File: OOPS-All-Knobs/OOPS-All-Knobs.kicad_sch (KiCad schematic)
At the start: 144 parts

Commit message: Added ground
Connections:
- net GND: now reaches ENC24.C
- net GND: now also ENC1.C, ENC10.C, ENC11.C, ENC12.C, ENC13.C, ENC14.C, ENC15.C, ENC16.C, ENC17.C, ENC18.C, ENC19.C, ENC2.C, ENC20.C, ENC21.C, ENC22.C, ENC23.C, ENC25.C, ENC26.C, ENC27.C, ENC28.C, ENC29.C, ENC3.C, ENC30.C, ENC31.C, ENC32.C, ENC33.C, ENC34.C, ENC35.C, ENC36.C, ENC37.C, ENC38.C, ENC39.C, ENC4.C, ENC40.C, ENC41.C, ENC42.C, ENC43.C, ENC44.C, ENC45.C, ENC46.C, ENC47.C, ENC48.C, ENC5.C, ENC6.C, ENC7.C, ENC8.C, ENC9.C

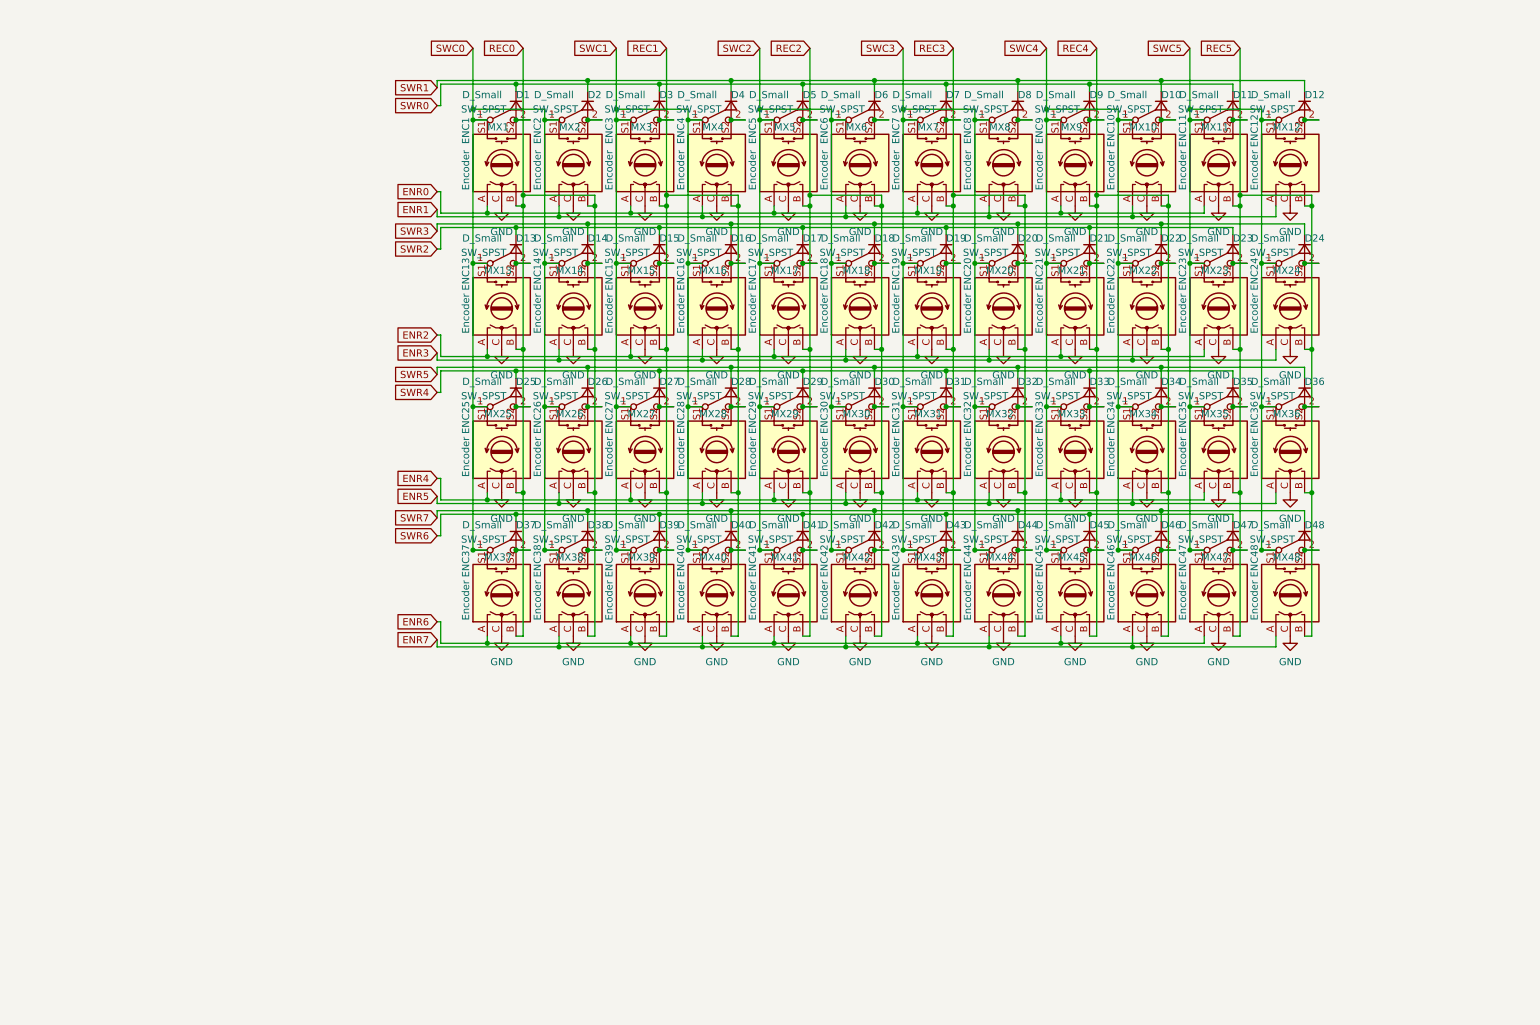
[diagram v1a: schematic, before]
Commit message: Placed and routed controller
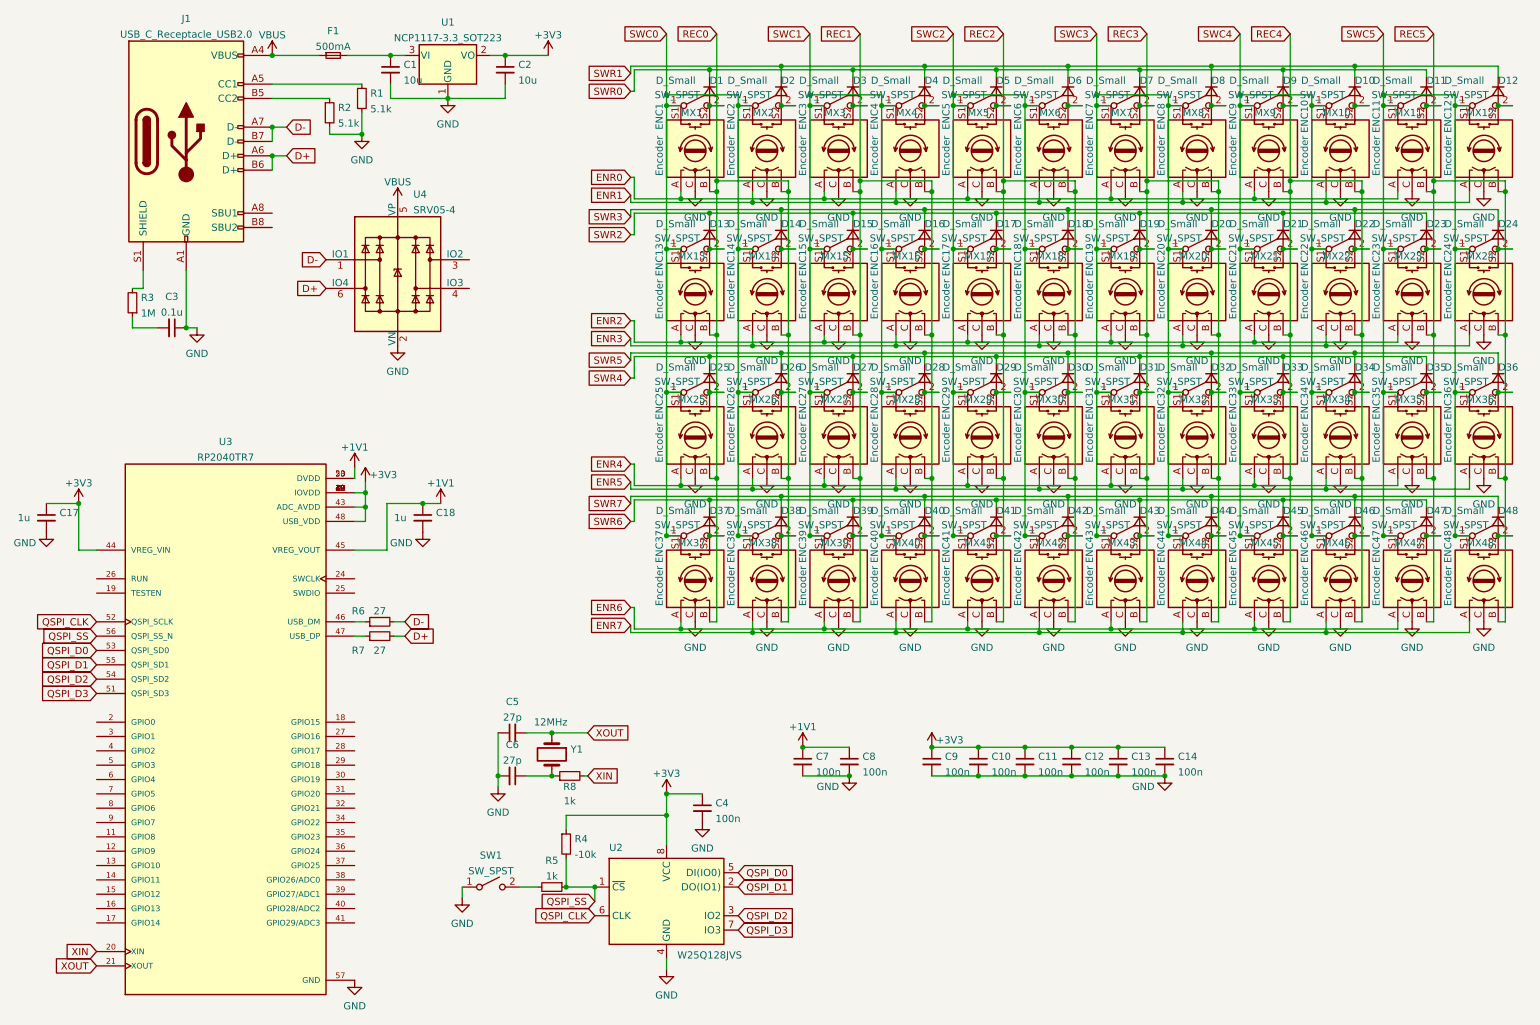
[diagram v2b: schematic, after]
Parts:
- added C1, C2: 10u, Capacitor_SMD:C_0402_1005Metric, symbol Device:C_Small
- added C10, C11, C12, C13, C14, C4, C7, C8, C9: 100n, Capacitor_SMD:C_0402_1005Metric, symbol Device:C_Small
- added C17, C18: 1u, Capacitor_SMD:C_0402_1005Metric, symbol Device:C_Small
- added C3: 0.1u, Capacitor_SMD:C_0402_1005Metric, symbol Device:C_Small
- added C5, C6: 27p, Capacitor_SMD:C_0402_1005Metric, symbol Device:C_Small
- added F1: 500mA, Fuse:Fuse_1206_3216Metric, symbol Device:Fuse_Small
- added J1: USB_C_Receptacle_USB2.0, Connector_USB:USB_C_Receptacle_HRO_TYPE-C-31-M-12, symbol Connector:USB_C_Receptacle_USB2.0
- added R1, R2: 5.1k, Resistor_SMD:R_0402_1005Metric, symbol Device:R_Small
- added R3: 1M, Resistor_SMD:R_0402_1005Metric, symbol Device:R_Small
- added R4: -10k, Resistor_SMD:R_0603_1608Metric, symbol Device:R_Small
- added R5, R8: 1k, Resistor_SMD:R_0402_1005Metric, symbol Device:R_Small
- added R6, R7: 27, Resistor_SMD:R_0402_1005Metric, symbol Device:R_Small
- added SW1: SW_SPST, Keebio-Parts:SW_SPST_TL3342, symbol Switch:SW_SPST
- added U1: NCP1117-3.3_SOT223, Package_TO_SOT_SMD:SOT-89-3, symbol Regulator_Linear:NCP1117-3.3_SOT223
- added U2: W25Q128JVS, Package_SO:SOIC-8_5.23x5.23mm_P1.27mm, symbol Memory_Flash:W25Q128JVS
- added U3: RP2040TR7, SnapEDA Library:QFN40P700X700X90-57N, symbol RP2040TR7:RP2040TR7
- added U4: SRV05-4, marbastlib-various:SOT-23-6-routable, symbol marbastlib-various:SRV05-4
- added Y1: 12MHz, Crystal:Crystal_SMD_3225-4Pin_3.2x2.5mm, symbol Device:Crystal
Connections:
- net GND: now also C1.2, C10.2, C11.2, C12.2, C13.2, C14.2, C17.2, C18.2, C2.2, C3.1, C4.2, C5.1, C6.2, C7.2, C8.2, C9.2, J1.A1 (GND), J1.A12 (GND), J1.B1 (GND), J1.B12 (GND), R1.2, R2.2, SW1.1 (A), U1.1 (GND), U2.4 (GND), U3.57 (GND), U4.2 (VN)
- new net: C1.1, F1.2, U1.3 (VI)
- new net: R5.2, SW1.2 (B)
- new net: C6.1, R8.1, Y1.2
- new net: R7.1, U3.47 (USB_DP)
- new net: C3.2, R3.1
- new net: J1.A5 (CC1), R1.1
- new net: J1.B5 (CC2), R2.1
- new net: J1.S1 (SHIELD), R3.2
- new net: R6.1, U3.46 (USB_DM)
- new net +1V1: C18.1, C7.1, C8.1, U3.23 (DVDD), U3.45 (VREG_VOUT), U3.50 (DVDD)
- new net +3V3: C10.1, C11.1, C12.1, C13.1, C14.1, C17.1, C2.1, C4.1, C9.1, R4.1, U1.2 (VO), U2.8 (VCC), U3.1 (IOVDD), U3.10 (IOVDD), U3.22 (IOVDD), U3.33 (IOVDD), U3.42 (IOVDD), U3.43 (ADC_AVDD), U3.44 (VREG_VIN), U3.48 (USB_VDD), U3.49 (IOVDD)
- new net D+: J1.A6 (D+), J1.B6 (D+), R7.2, U4.6 (IO4)
- new net D-: J1.A7 (D-), J1.B7 (D-), R6.2, U4.1 (IO1)
- new net QSPI_CLK: U2.6 (CLK), U3.52 (QSPI_SCLK)
- new net QSPI_D0: U2.5 (DI(IO0)), U3.53 (QSPI_SD0)
- new net QSPI_D1: U2.2 (DO(IO1)), U3.55 (QSPI_SD1)
- new net QSPI_D2: U2.3 (IO2), U3.54 (QSPI_SD2)
- new net QSPI_D3: U2.7 (IO3), U3.51 (QSPI_SD3)
- new net QSPI_SS: R4.2, R5.1, U2.1 (~{CS}), U3.56 (QSPI_SS_N)
- new net VBUS: F1.1, J1.A4 (VBUS), J1.A9 (VBUS), J1.B4 (VBUS), J1.B9 (VBUS), U4.5 (VP)
- new net XIN: R8.2, U3.20 (XIN)
- new net XOUT: C5.2, U3.21 (XOUT), Y1.1
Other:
- moved on the sheet: D1, D10, D11, D12, D13, D14, D15, D16, D17, D18, D19, D2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

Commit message: Some progress on routing matrices
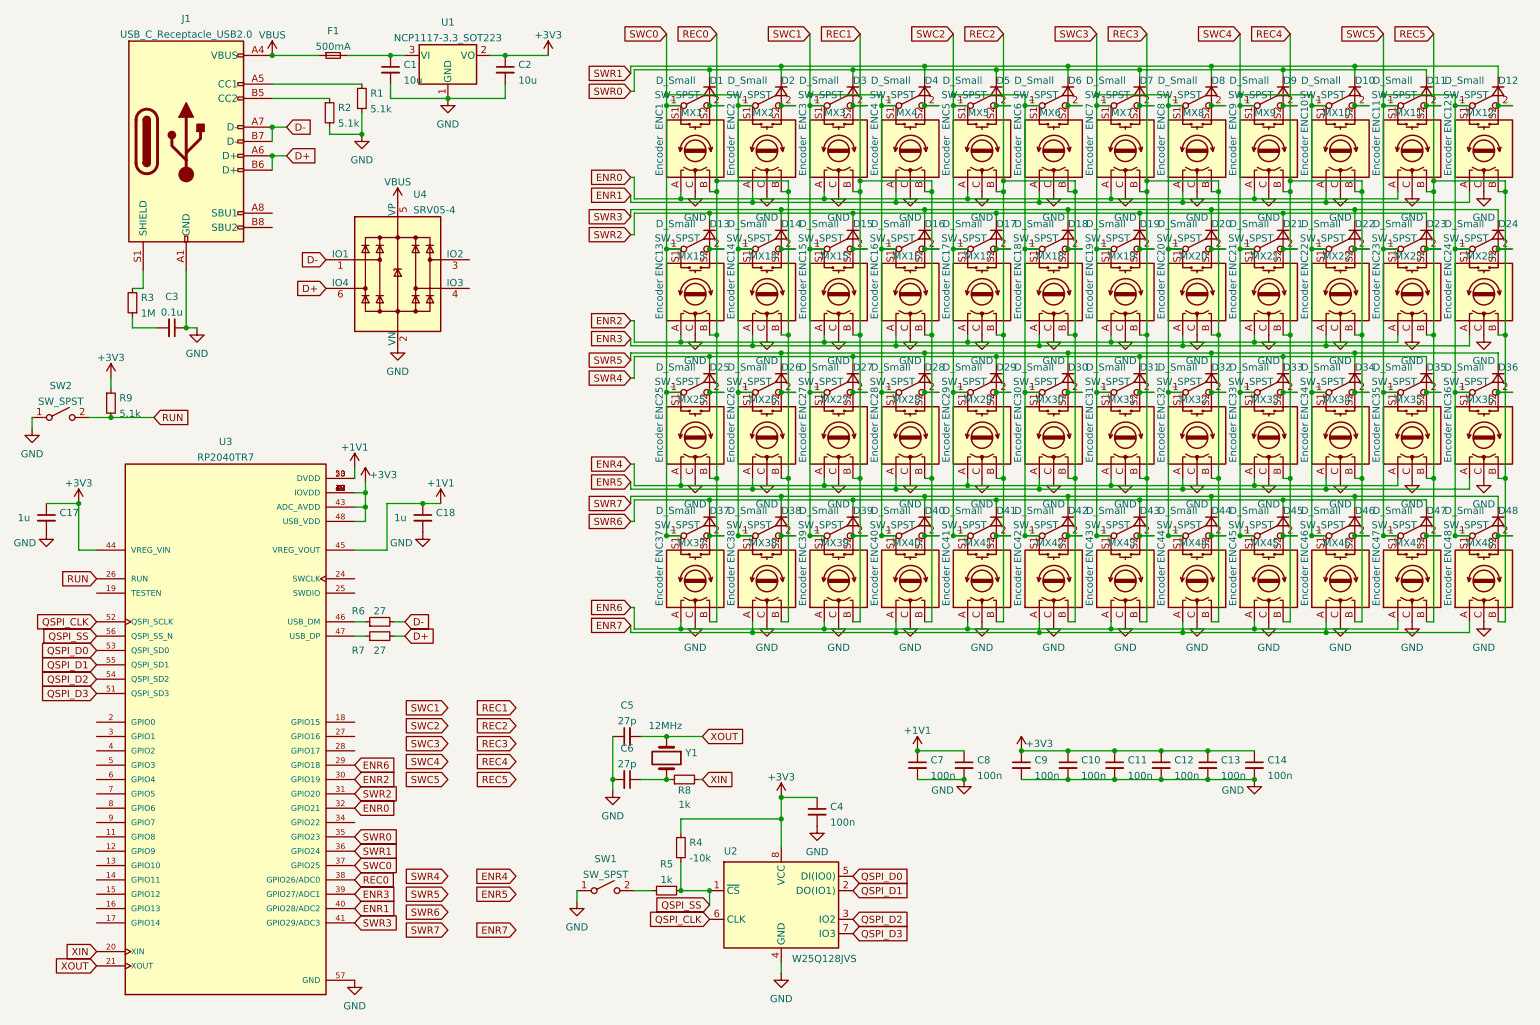
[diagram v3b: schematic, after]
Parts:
- added R9: 5.1k, Resistor_SMD:R_0402_1005Metric, symbol Device:R_Small
- added SW2: SW_SPST, Keebio-Parts:SW_SPST_TL3342, symbol Switch:SW_SPST
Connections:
- net +3V3: now also R9.1
- net ENR0: now also U3.32 (GPIO21)
- net ENR1: now also U3.40 (GPIO28/ADC2)
- net ENR2: now also U3.30 (GPIO19)
- net ENR3: now also U3.39 (GPIO27/ADC1)
- net ENR6: now also U3.29 (GPIO18)
- net GND: now also SW2.1 (A)
- net REC0: now also U3.38 (GPIO26/ADC0)
- net SWC0: now also U3.37 (GPIO25)
- net SWR0: now also U3.35 (GPIO23)
- net SWR1: now also U3.36 (GPIO24)
- net SWR2: now also U3.31 (GPIO20)
- net SWR3: now also U3.41 (GPIO29/ADC3)
- net RUN: now reaches U3.26 (RUN)
- net RUN: now also R9.2, SW2.2 (B)
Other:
- moved on the sheet: C10, C11, C12, C13, C14, C4, C5, C6, C7, C8, C9, R4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

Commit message: routed controller, just a few connections left
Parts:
- added J2: Conn_01x03_Female, Connector_PinHeader_2.54mm:PinHeader_1x03_P2.54mm_Vertical, symbol Connector:Conn_01x03_Female
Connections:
- net ENR4: now also U3.15 (GPIO12)
- net ENR5: now also U3.14 (GPIO11)
- net ENR7: now also U3.17 (GPIO14)
- net GND: now also J2.2 (Pin_2)
- net REC1: now also U3.5 (GPIO3)
- net REC2: now also U3.4 (GPIO2)
- net REC3: now also U3.7 (GPIO5)
- net REC4: now also U3.8 (GPIO6)
- net REC5: now also U3.12 (GPIO9)
- net SWC1: now also U3.2 (GPIO0)
- net SWC2: now also U3.3 (GPIO1)
- net SWC3: now also U3.6 (GPIO4)
- net SWC4: now also U3.11 (GPIO8)
- net SWC5: now also U3.13 (GPIO10)
- net SWR4: now also U3.27 (GPIO16)
- net SWR5: now also U3.28 (GPIO17)
- net SWR6: now also U3.16 (GPIO13)
- net SWR7: now also U3.18 (GPIO15)
- net SWCLK: now reaches U3.24 (SWCLK)
- net SWCLK: now also J2.1 (Pin_1)
- net SWDIO: now reaches U3.25 (SWDIO)
- net SWDIO: now also J2.3 (Pin_3)
